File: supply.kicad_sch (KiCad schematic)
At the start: 12 parts, among them U3 TLV70012_SC70, U4 TLV70025_SC70, U5 TLV70033_SC70

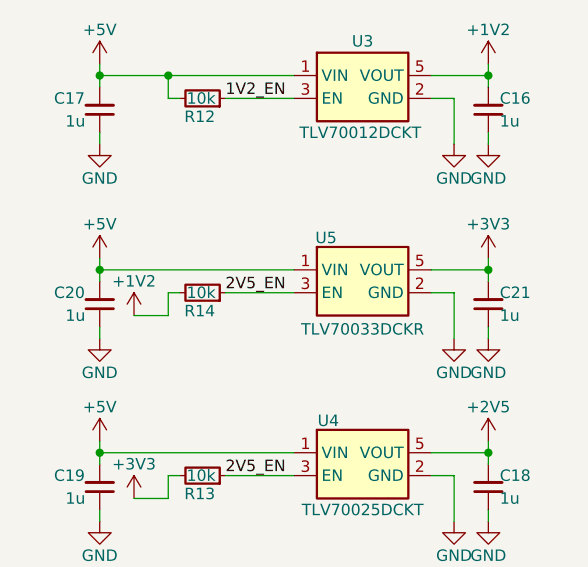
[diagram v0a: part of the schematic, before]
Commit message: [#72133] Add rough schematic hierarchy
Signed-off-by: Dawid Lentka <dlentka@antmicro.com>
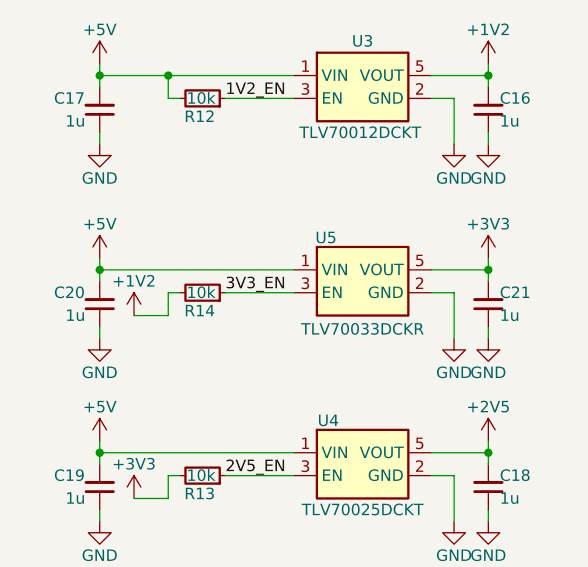
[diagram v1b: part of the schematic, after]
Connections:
- net 2V5_EN: no longer R14.1, U5.3 (EN)
- new net 3V3_EN: R14.1, U5.3 (EN)
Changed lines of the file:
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@@
 		)
 	)
-	(label "2V5_EN"
+	(label "3V3_EN"
 		(at 109.22 110.49 0)
 		(fields_autoplaced yes)

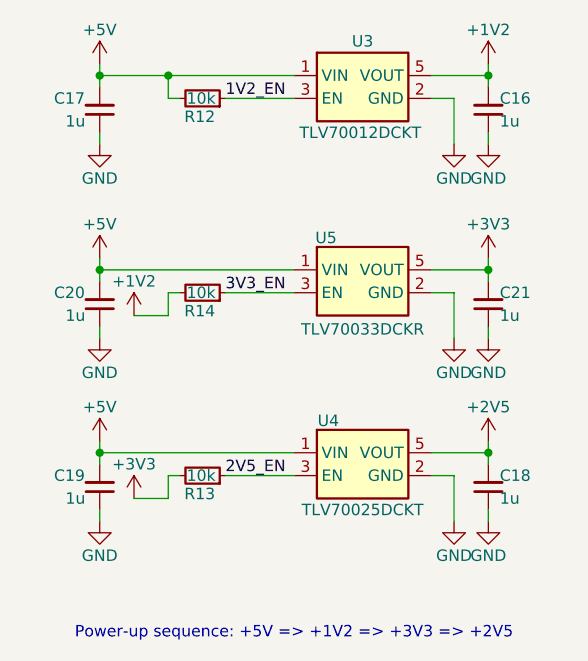
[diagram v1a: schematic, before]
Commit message: [#72133] Move executor switching to new scheet; Add FPGA flash programmer
Signed-off-by: Dawid Lentka <dlentka@antmicro.com>
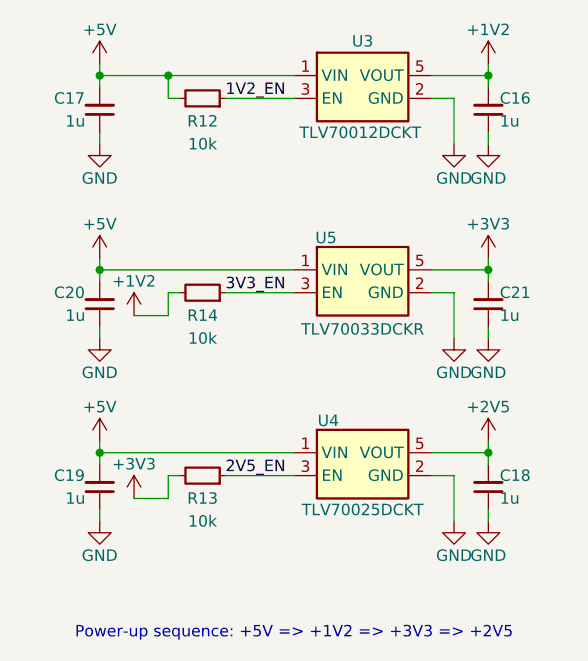
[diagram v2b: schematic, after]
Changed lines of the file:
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@@
 		(dnp no)
 		(property "Reference" "R14"
-			(at 104.648 112.522 0)
-			(effects
-				(font
-					(size 1.27 1.27)
-					(thickness 0.15)
-				)
-				(justify right)
+			(at 106.68 113.03 0)
+			(effects
+				(font
+					(size 1.27 1.27)
+					(thickness 0.15)
+				)
 			)
 		)
@@
 		)
 		(property "Val" "10k"
-			(at 104.902 110.49 0)
-			(effects
-				(font
-					(size 1.27 1.27)
-					(thickness 0.15)
-				)
-				(justify right)
+			(at 106.68 115.57 0)
+			(effects
+				(font
+					(size 1.27 1.27)
+					(thickness 0.15)
+				)
 			)
 		)
@@
 		(dnp no)
 		(property "Reference" "R13"
-			(at 104.648 132.842 0)
-			(effects
-				(font
-					(size 1.27 1.27)
-					(thickness 0.15)
-				)
-				(justify right)
+			(at 106.68 133.35 0)
+			(effects
+				(font
+					(size 1.27 1.27)
+					(thickness 0.15)
+				)
 			)
 		)
@@
 		)
 		(property "Val" "10k"
-			(at 104.902 130.81 0)
-			(effects
-				(font
-					(size 1.27 1.27)
-					(thickness 0.15)
-				)
-				(justify right)
+			(at 106.68 135.89 0)
+			(effects
+				(font
+					(size 1.27 1.27)
+					(thickness 0.15)
+				)
 			)
 		)
@@
 		(dnp no)
 		(property "Reference" "R12"
-			(at 104.648 90.932 0)
-			(effects
-				(font
-					(size 1.27 1.27)
-					(thickness 0.15)
-				)
-				(justify right)
+			(at 106.68 91.44 0)
+			(effects
+				(font
+					(size 1.27 1.27)
+					(thickness 0.15)
+				)
 			)
 		)
@@
 		)
 		(property "Val" "10k"
-			(at 104.902 88.9 0)
-			(effects
-				(font
-					(size 1.27 1.27)
-					(thickness 0.15)
-				)
-				(justify right)
-			)
-		)
+			(at 106.68 93.98 0)
+			(effects
+				(font
+					(size 1.27 1.27)
+					(thickness 0.15)
+				)
+			)
+		)

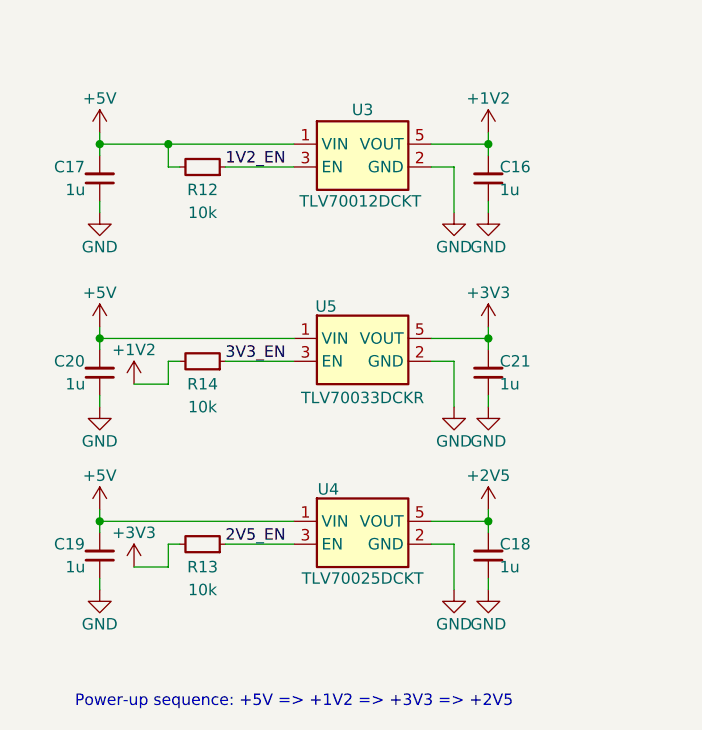
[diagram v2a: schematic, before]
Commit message: [#72133] Unify sheet size
Signed-off-by: Dawid Lentka <dlentka@antmicro.com>
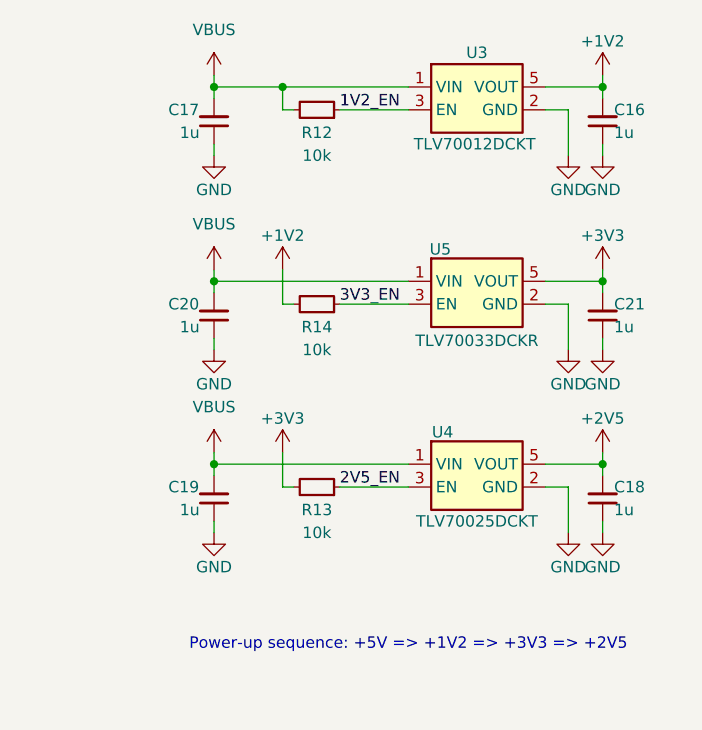
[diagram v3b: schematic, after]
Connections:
- net +5V renamed VBUS
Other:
- title: LED Panel -> LED Panel Board
- moved on the sheet: C16, C17, C18, C19, C20, C21, R12, R13, R14, U3, U4, U5

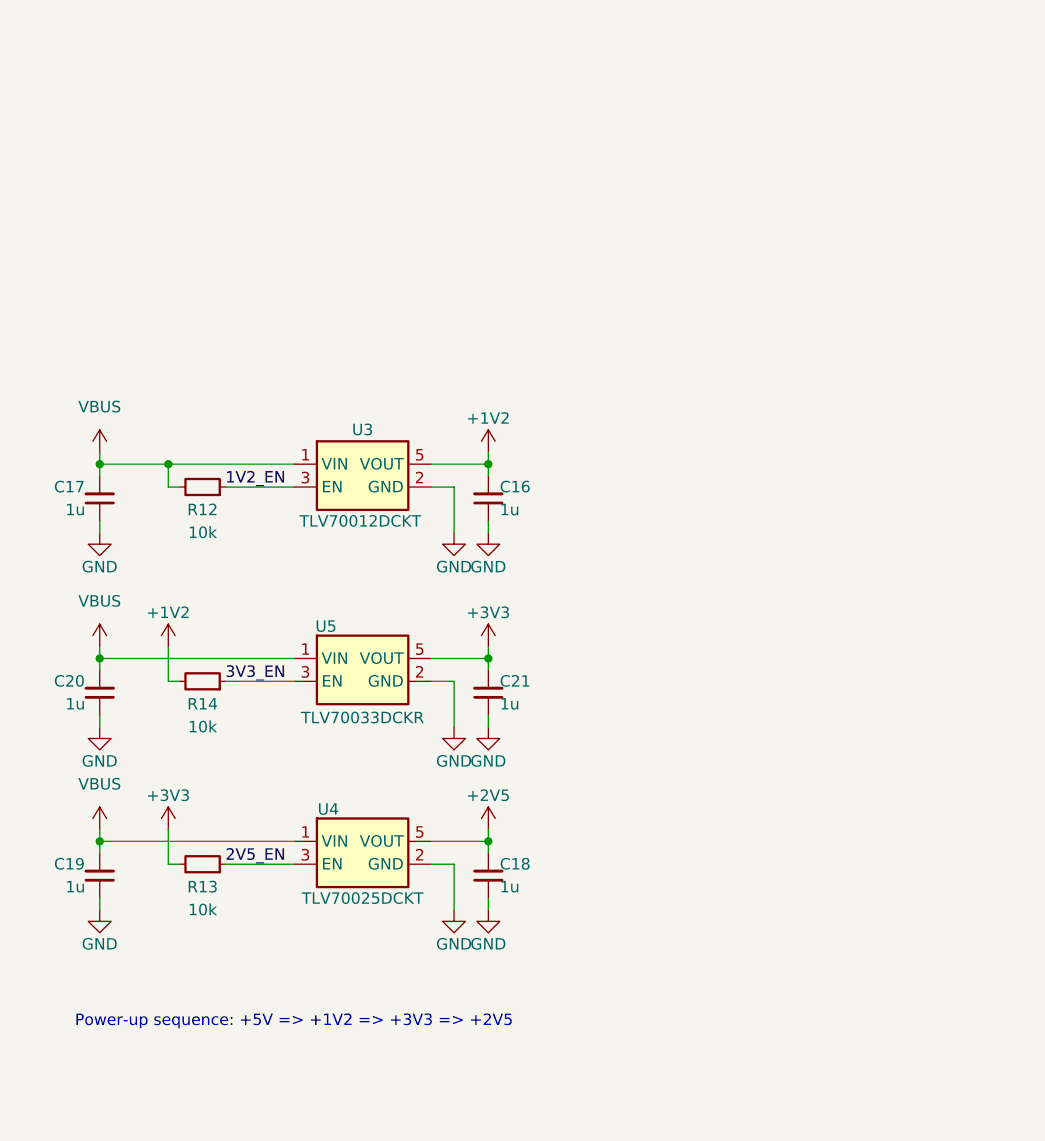
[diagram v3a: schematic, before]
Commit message: [#72133] Add indicator LEDs & testpoints
Signed-off-by: Dawid Lentka <dlentka@antmicro.com>
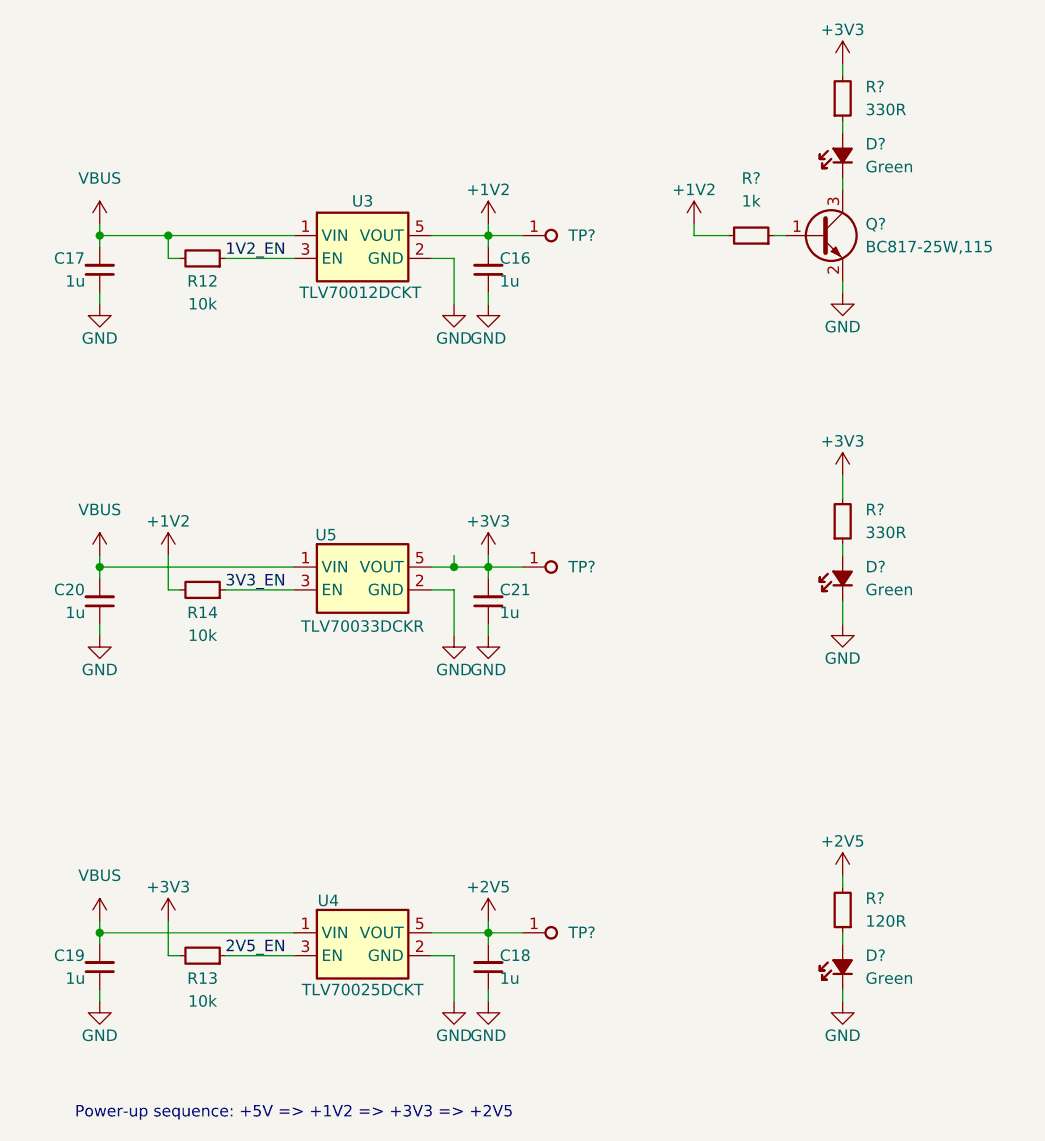
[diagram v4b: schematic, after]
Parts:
- added D? (x3): LED_G_0603_KP-1608CGCK, antmicro-footprints:LED_0603_1608Metric_G, symbol antmicroLEDIndicationDiscrete:LED_G_0603_KP-1608CGCK
- added Q?: BC817-25W, antmicro-footprints:SOT-323, symbol antmicroTransistorsBipolarSingle:BC817-25W
- added R? (x2): R_330R_0402, antmicro-footprints:R_0402_1005Metric, symbol antmicroResistors0402:R_330R_0402
- added R?: R_120R_0402, antmicro-footprints:R_0402_1005Metric, symbol antmicroResistors0402:R_120R_0402
- added R?: R_1k_0402, antmicro-footprints:R_0402_1005Metric, symbol antmicroResistors0402:R_1k_0402
- added TP? (x3): TP_0.75mm_SMD, antmicro-footprints:TP_SMD_0.75mm, symbol antmicroTestPoints:TP_0.75mm_SMD
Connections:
- net +1V2: now also R?.2, TP?.1
- net +2V5: now also R?.2, TP?.1
- net +3V3: now also R?.2, R?.2, TP?.1
- net GND: now also D?.1 (C), D?.1 (C), Q?.2 (E)
- new net: D?.1 (C), Q?.3 (C)
- new net: D?.2 (A), R?.1 (x3)
- new net: Q?.1 (B), R?.1
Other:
- moved on the sheet: C16, C17, C18, C19, C20, C21, R12, R13, R14, U3, U4, U5

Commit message: [#72133] Annotate schematics
Signed-off-by: Dawid Lentka <dlentka@antmicro.com>
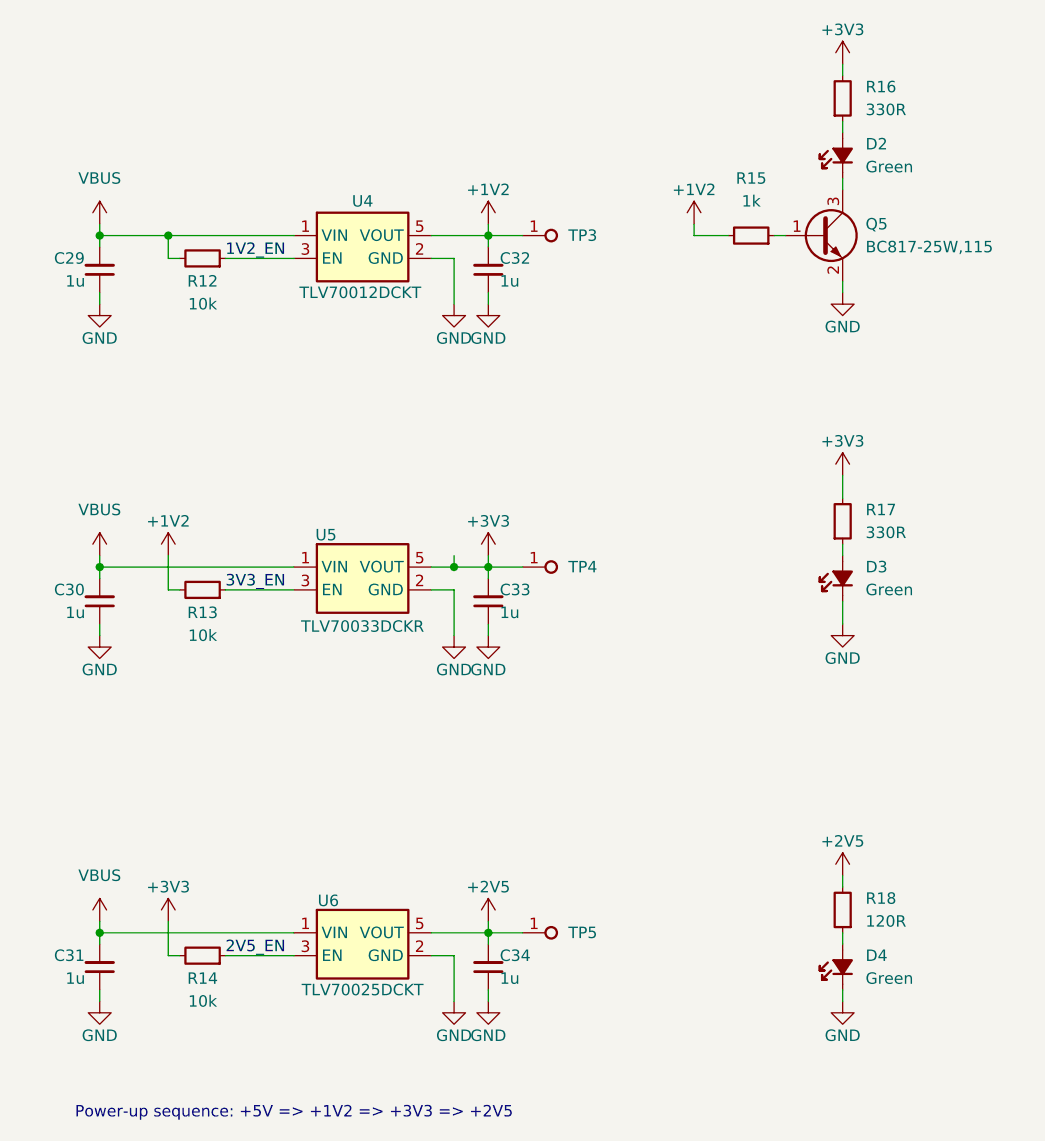
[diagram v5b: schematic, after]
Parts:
- gave numbers to parts that had none: 11
- renumbered C17 to C29, C20 to C30, C19 to C31, C16 to C32, C21 to C33, C18 to C34, R14 to R13, R13 to R14, U3 to U4, U4 to U6
